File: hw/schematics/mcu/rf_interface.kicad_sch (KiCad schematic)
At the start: 3 parts

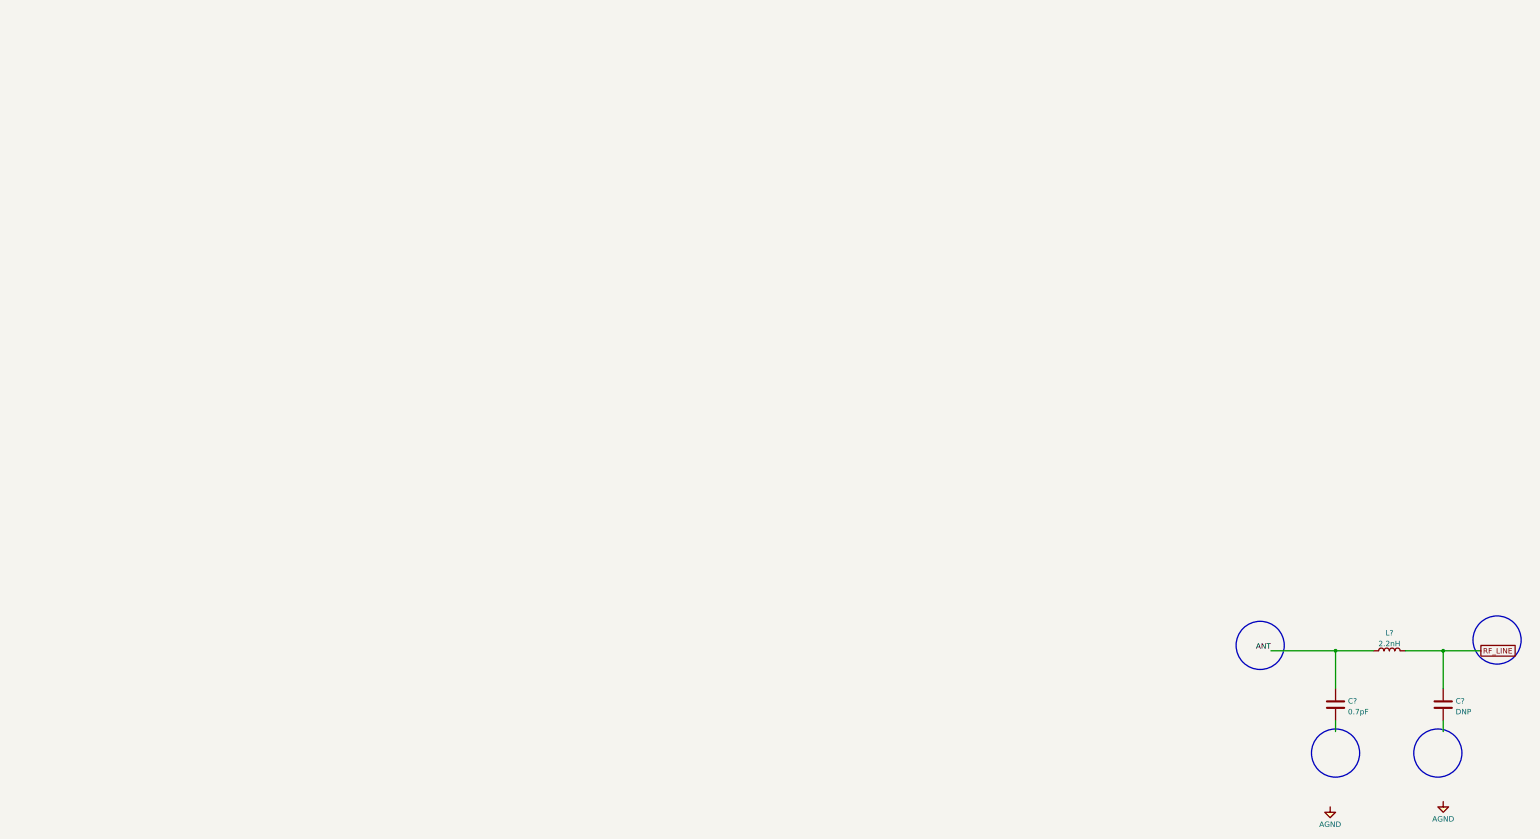
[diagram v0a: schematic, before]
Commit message: 
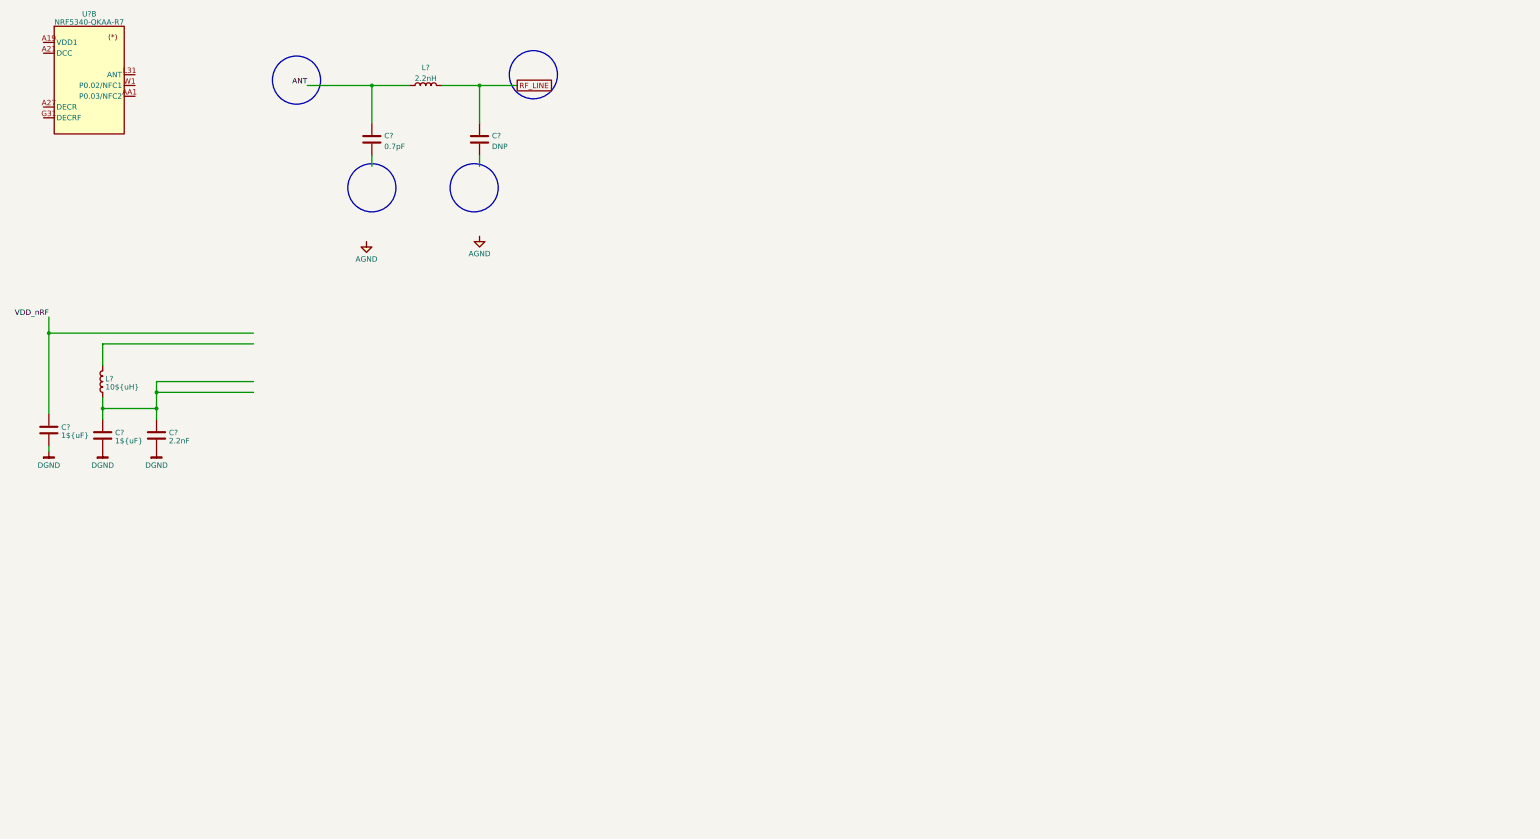
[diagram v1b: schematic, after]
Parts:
- added C? (x2): 1${uF}, symbol Device:C
- added C?: 2.2nF, symbol Device:C
- added L?: 10${uH}, symbol Device:L
- added U?: NRF5340-QKAA-R7, 0:NRF5340-QKAA-R7, symbol 1.Embedded.Specialized:NRF5340-QKAA-R7
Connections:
- new net: C?.1, C?.1, L?.1
- new net DGND: C?.2, C?.2, C?.2
- new net VDD_nRF: C?.1
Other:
- moved on the sheet: C?, L?
